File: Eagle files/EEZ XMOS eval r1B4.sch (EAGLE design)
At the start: 223 parts, among them IC1 TPS61169DCKR, IC10 IS42S16400J, IC11 SN74CBTLV3257, IC12 SN74LVC1G02DBVR, IC13 AT25SF041-SSHDT, IC14 SN74CBTLV3257, IC15 TPS2051BDBVR, IC16 TPD2E001DZDR, IC17 TPS561208DDCR, IC18 XE216-512-TQ128-C20, IC19 TPD4E001DRLR, IC2 TPS561208DDCR, IC20 TPD4E001DRLR, IC21 74LVC1G07SE-7, IC22 74LVC1G07SE-7, IC23 TPA6205A1DGN, IC24 DP83848CVV/NOPB, IC25 M95256-WMN6P, IC26 74VHC595MTC, IC27 PCA21125T/Q900/1,1, IC28 MCP23S17-E/SS, IC3 74VHC595MTC, IC4 TPS561208DDCR, IC5 74VHC595MTC, IC6 TPS3808G33DBVR, IC7 AR1021-I/SS, IC8 TPS3808G09DBVR, IC9 74AUP1G74DC.125, J1 678038020, J2 5033981892, Q1 IRLML2246TRPBF, SW1 1301.9316, X1 FC68149, X2 SSW-105-02-S-D, X3 TSW-104-02-S-D_NN, X4 TSW-103-07-F-D, X5 ZL231-20KG, X6 22-23-2021, X7 LMJTAB881243M-L, X8 SSW-107-02-S-D, X9 PCA-6G-20-HL-3 or 52746-2071, Y1 XTAL016178- 85SMX

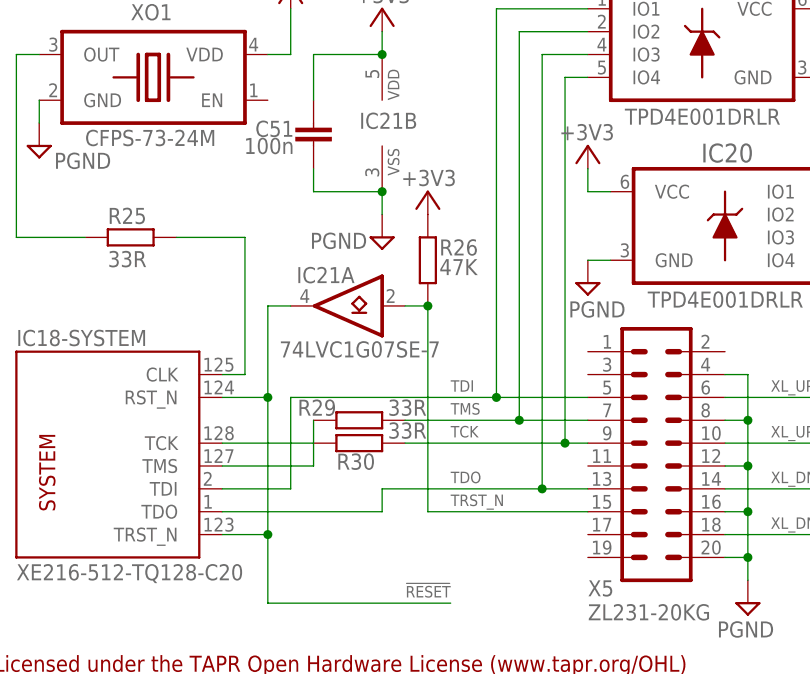
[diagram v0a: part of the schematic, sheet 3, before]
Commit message: pin swap on X3
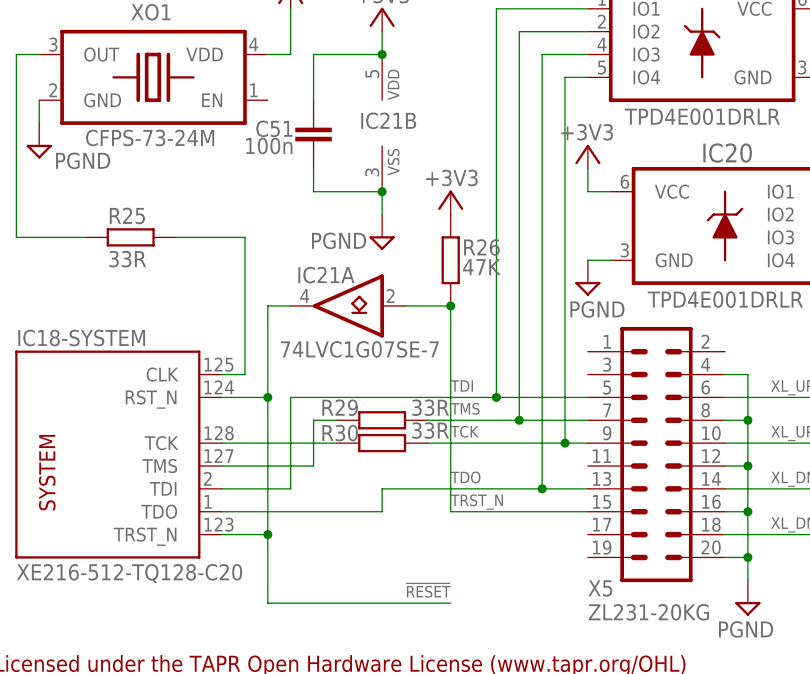
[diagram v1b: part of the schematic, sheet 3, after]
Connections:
- net LATCH_IN: now also X3-2.1; no longer X3-5.1
- net X0D05/QS_D1: now also X3-5.1; no longer X3-2.1
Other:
- moved on the sheet: R26, R29, R30, X3-2
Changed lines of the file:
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@@
 <attribute name="NAME" x="250.19" y="56.769" size="1.778" layer="95" rot="MR180"/>
-</instance>
-<instance part="X3" gate="-5" x="243.84" y="50.8" smashed="yes" rot="R180">
-<attribute name="NAME" x="250.19" y="49.911" size="1.778" layer="95"/>
-</instance>
-<instance part="X3" gate="-2" x="243.84" y="58.42" smashed="yes" rot="MR0">
-<attribute name="NAME" x="250.19" y="59.309" size="1.778" layer="95" rot="MR180"/>
 </instance>
 <instance part="X3" gate="-1" x="243.84" y="60.96" smashed="yes" rot="R180">
@@
 </instance>
 <instance part="X3" gate="-8" x="243.84" y="43.18" rot="R180"/>
+<instance part="X3" gate="-5" x="243.84" y="50.8" smashed="yes" rot="R180">
+<attribute name="NAME" x="250.19" y="49.911" size="1.778" layer="95"/>
+</instance>
+<instance part="X3" gate="-2" x="243.84" y="58.42" smashed="yes" rot="R180">
+<attribute name="NAME" x="250.19" y="57.531" size="1.778" layer="95"/>
+</instance>
 </instances>
 <busses>
@@
 </segment>
 <segment>
-<pinref part="X3" gate="-2" pin="1"/>
-<wire x1="243.84" y1="58.42" x2="226.06" y2="58.42" width="0.1524" layer="91"/>
-<label x="226.06" y="59.055" size="1.27" layer="102"/>
+<wire x1="243.84" y1="50.8" x2="226.06" y2="50.8" width="0.1524" layer="91"/>
+<label x="226.06" y="51.435" size="1.27" layer="102"/>
+<pinref part="X3" gate="-5" pin="1"/>
 </segment>
 </net>
@@
 <net name="LATCH_IN" class="0">
 <segment>
-<pinref part="X3" gate="-5" pin="1"/>
-<wire x1="243.84" y1="50.8" x2="226.06" y2="50.8" width="0.1524" layer="91"/>
-<label x="226.06" y="51.435" size="1.27" layer="102"/>
+<wire x1="243.84" y1="58.42" x2="226.06" y2="58.42" width="0.1524" layer="91"/>
+<label x="226.06" y="59.055" size="1.27" layer="102"/>
+<pinref part="X3" gate="-2" pin="1"/>
 </segment>
 <segment>
@@
 <attribute name="VALUE" x="236.855" y="46.228" size="1.778" layer="96"/>
 </instance>
-<instance part="R26" gate="G$1" x="50.8" y="53.34" smashed="yes" rot="R270">
-<attribute name="NAME" x="52.07" y="55.6514" size="1.778" layer="95" rot="MR180"/>
-<attribute name="VALUE" x="52.07" y="53.467" size="1.778" layer="96" rot="MR180"/>
-</instance>
-<instance part="+3V2" gate="G$1" x="50.8" y="60.96" smashed="yes">
-<attribute name="VALUE" x="53.975" y="61.595" size="1.778" layer="96" rot="MR0"/>
+<instance part="R26" gate="G$1" x="53.34" y="53.34" smashed="yes" rot="R270">
+<attribute name="NAME" x="54.61" y="55.6514" size="1.778" layer="95" rot="MR180"/>
+<attribute name="VALUE" x="54.61" y="53.467" size="1.778" layer="96" rot="MR180"/>
+</instance>
+<instance part="+3V2" gate="G$1" x="53.34" y="60.96" smashed="yes">
+<attribute name="VALUE" x="56.515" y="61.595" size="1.778" layer="96" rot="MR0"/>
 </instance>
 <instance part="IC21" gate="A" x="43.18" y="48.26" smashed="yes" rot="MR0">
@@
 <attribute name="VALUE" x="66.421" y="46.99" size="1.778" layer="96"/>
 </instance>
-<instance part="R29" gate="G$1" x="43.18" y="35.56" smashed="yes">
-<attribute name="NAME" x="40.64" y="36.068" size="1.778" layer="95" rot="MR0"/>
-<attribute name="VALUE" x="46.355" y="36.068" size="1.778" layer="96"/>
-</instance>
-<instance part="R30" gate="G$1" x="43.18" y="33.02" smashed="yes">
-<attribute name="NAME" x="40.64" y="30.0736" size="1.778" layer="95"/>
-<attribute name="VALUE" x="46.355" y="33.528" size="1.778" layer="96"/>
+<instance part="R29" gate="G$1" x="45.72" y="35.56" smashed="yes">
+<attribute name="NAME" x="43.18" y="36.068" size="1.778" layer="95" rot="MR0"/>
+<attribute name="VALUE" x="48.895" y="36.068" size="1.778" layer="96"/>
+</instance>
+<instance part="R30" gate="G$1" x="45.72" y="33.02" smashed="yes">
+<attribute name="NAME" x="43.18" y="33.2486" size="1.778" layer="95" rot="MR0"/>
+<attribute name="VALUE" x="48.895" y="33.528" size="1.778" layer="96"/>
 </instance>
 <instance part="X4" gate="-4" x="254" y="76.2" smashed="yes" rot="R180">
@@
 <label x="53.34" y="36.195" size="1.27" layer="102"/>
 <wire x1="68.58" y1="35.56" x2="60.96" y2="35.56" width="0.1524" layer="91"/>
-<wire x1="60.96" y1="35.56" x2="48.26" y2="35.56" width="0.1524" layer="91"/>
+<wire x1="60.96" y1="35.56" x2="50.8" y2="35.56" width="0.1524" layer="91"/>
 <pinref part="IC19" gate="G$1" pin="IO2"/>
 <wire x1="68.58" y1="78.74" x2="60.96" y2="78.74" width="0.1524" layer="91"/>
@@
 <junction x="66.04" y="33.02"/>
 <pinref part="R30" gate="G$1" pin="2"/>
-<wire x1="48.26" y1="33.02" x2="66.04" y2="33.02" width="0.1524" layer="91"/>
+<wire x1="50.8" y1="33.02" x2="66.04" y2="33.02" width="0.1524" layer="91"/>
 </segment>
 </net>
@@
 <segment>
 <pinref part="X5" gate="1" pin="15"/>
-<wire x1="68.58" y1="25.4" x2="50.8" y2="25.4" width="0.1524" layer="91"/>
-<wire x1="50.8" y1="25.4" x2="50.8" y2="48.26" width="0.1524" layer="91"/>
+<wire x1="68.58" y1="25.4" x2="53.34" y2="25.4" width="0.1524" layer="91"/>
+<wire x1="53.34" y1="25.4" x2="53.34" y2="48.26" width="0.1524" layer="91"/>
 <pinref part="R26" gate="G$1" pin="2"/>
-<wire x1="50.8" y1="48.26" x2="48.26" y2="48.26" width="0.1524" layer="91"/>
-<junction x="50.8" y="48.26"/>
+<wire x1="53.34" y1="48.26" x2="48.26" y2="48.26" width="0.1524" layer="91"/>
+<junction x="53.34" y="48.26"/>
 <pinref part="IC21" gate="A" pin="A"/>
 <label x="53.34" y="26.035" size="1.27" layer="102"/>
@@
 <wire x1="27.94" y1="30.48" x2="38.1" y2="30.48" width="0.1524" layer="91"/>
 <wire x1="38.1" y1="30.48" x2="38.1" y2="35.56" width="0.1524" layer="91"/>
+<wire x1="38.1" y1="35.56" x2="40.64" y2="35.56" width="0.1524" layer="91"/>
 </segment>
 </net>
@@
 <pinref part="R30" gate="G$1" pin="1"/>
 <pinref part="IC18" gate="-SYSTEM" pin="TCK"/>
-<wire x1="38.1" y1="33.02" x2="27.94" y2="33.02" width="0.1524" layer="91"/>
-</segment>
-</net>
+<wire x1="40.64" y1="33.02" x2="27.94" y2="33.02" width="0.1524" layer="91"/>
+</segment>
+</net>

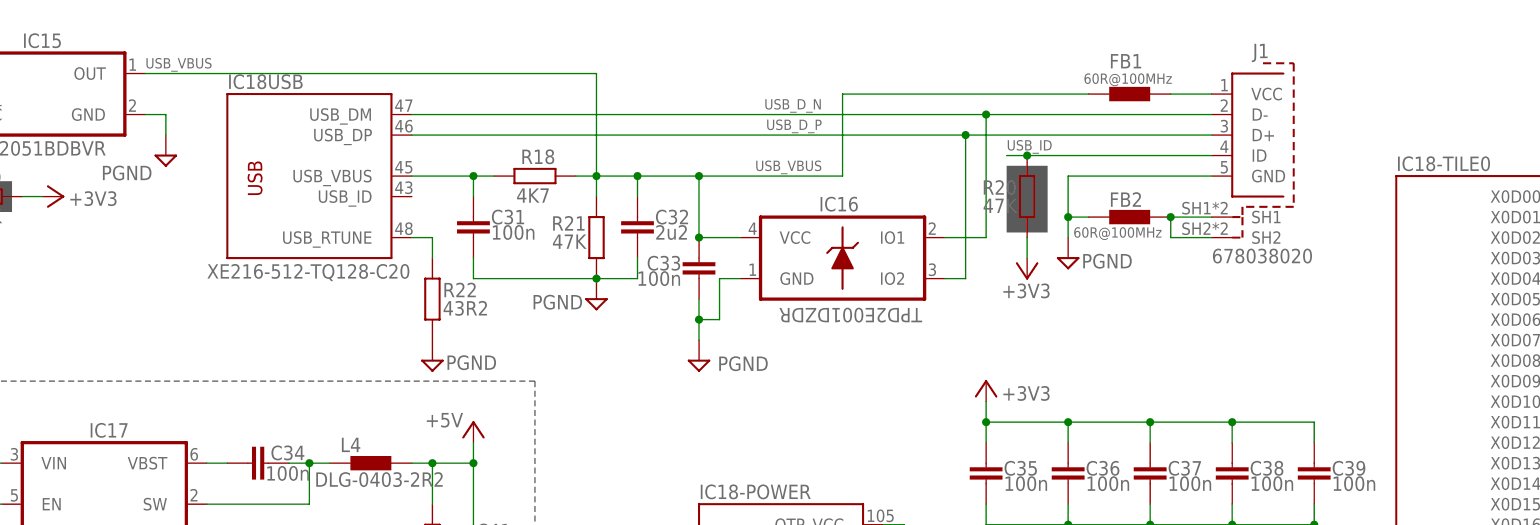
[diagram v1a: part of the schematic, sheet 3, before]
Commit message: BOM first version, added R67 as test point
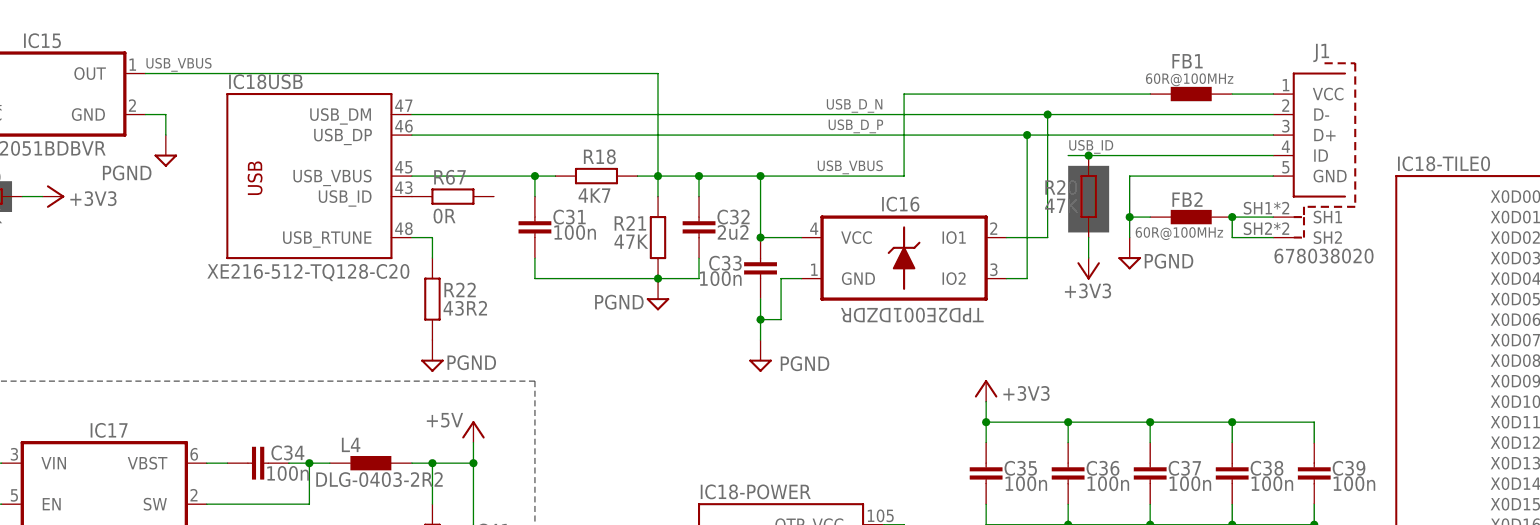
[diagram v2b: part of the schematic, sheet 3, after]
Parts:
- added R67: 0R, rcl:R-EU_R0805
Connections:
- new net N$18: IC18USB.USB_ID, R67.1
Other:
- note added: "4.3", 480x272, resistive touch screen"
- note added: "Consumption: +3.3 V, max. 33 mA; +32 V, 20 mA"
- note added: "LCD display: RFE43BH-AIW-DNS"
- note removed: "Consumption: +3.3 V, max. 33 mA; 32V, 20 mA"
- moved on the sheet: C31, C32, C33, FB1, FB2, IC16, J1, R18, R20, R21

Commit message: .brd file optimization
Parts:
- removed IC25: M95256-WMN6P, MyLib6:AT25XXXSOIC8
- added IC29: M95256-WMN6P, EEZ_Lib1:AT25XXXSOIC8
- FB1, FB2, FB3: device MyLib6:FERRITE_BEAD0603 -> EEZ_Lib1:FERRITE_BEAD0603
- IC27: device MyLib6:PCA21125TSSOP-14 -> EEZ_Lib1:PCA21125TSSOP-14
- Q1: device MyLib6:IRLML2246TRPBF -> EEZ_Lib1:IRLML2246TRPBF
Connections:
- net !SPI1_EEPROM: now also IC29.!CS; no longer IC25.!CS
- net +3V3: now also IC29.!HOLD, IC29.!WP, IC29.VCC; no longer IC25.!HOLD, IC25.!WP, IC25.VCC
- net GND: now also IC29.GND; no longer IC25.GND
- net SPI1_CLK: now also IC29.SCK; no longer IC25.SCK
- net SPI1_MISO: now also IC29.SO; no longer IC25.SO
- net SPI1_MOSI: now also IC29.SI; no longer IC25.SI
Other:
- moved on the sheet: IC27
